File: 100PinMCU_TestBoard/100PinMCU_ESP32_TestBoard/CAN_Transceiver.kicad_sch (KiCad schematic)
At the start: 9 parts, among them IC1 TCAN3413DR

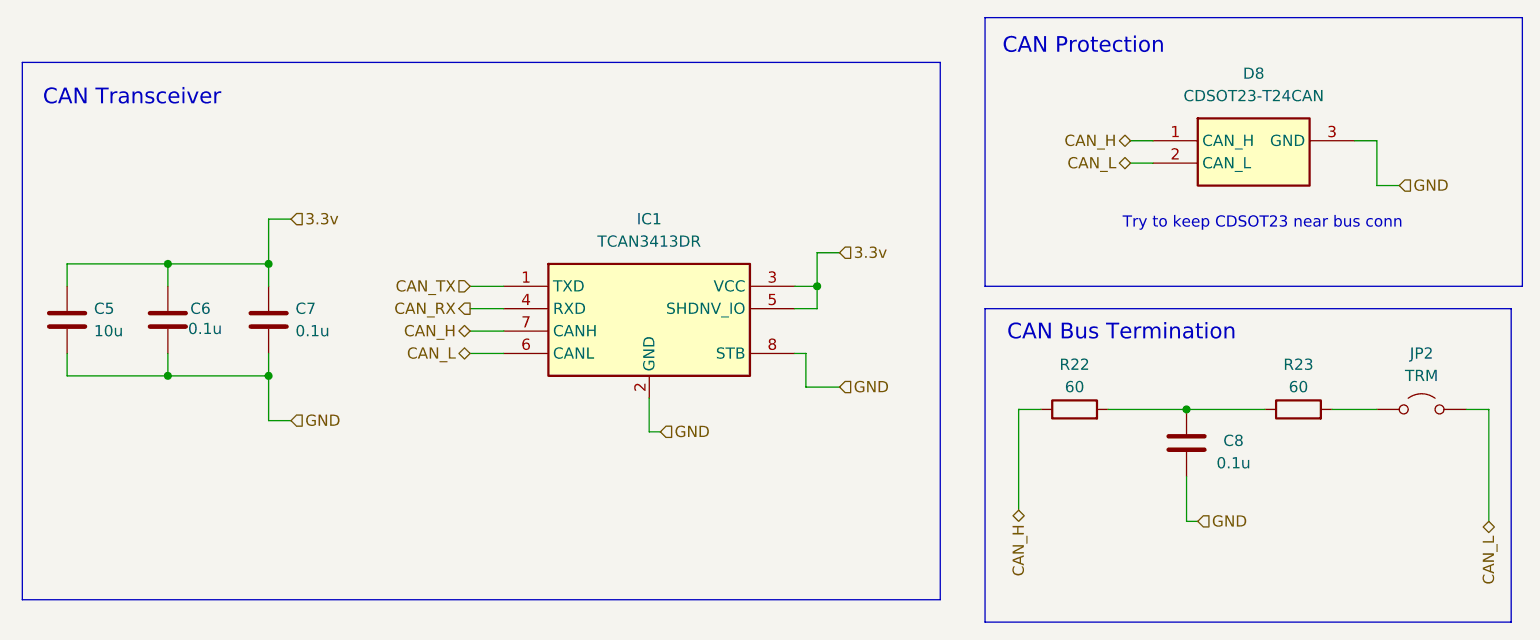
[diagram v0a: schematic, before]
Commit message: esp32 design block will be updated later
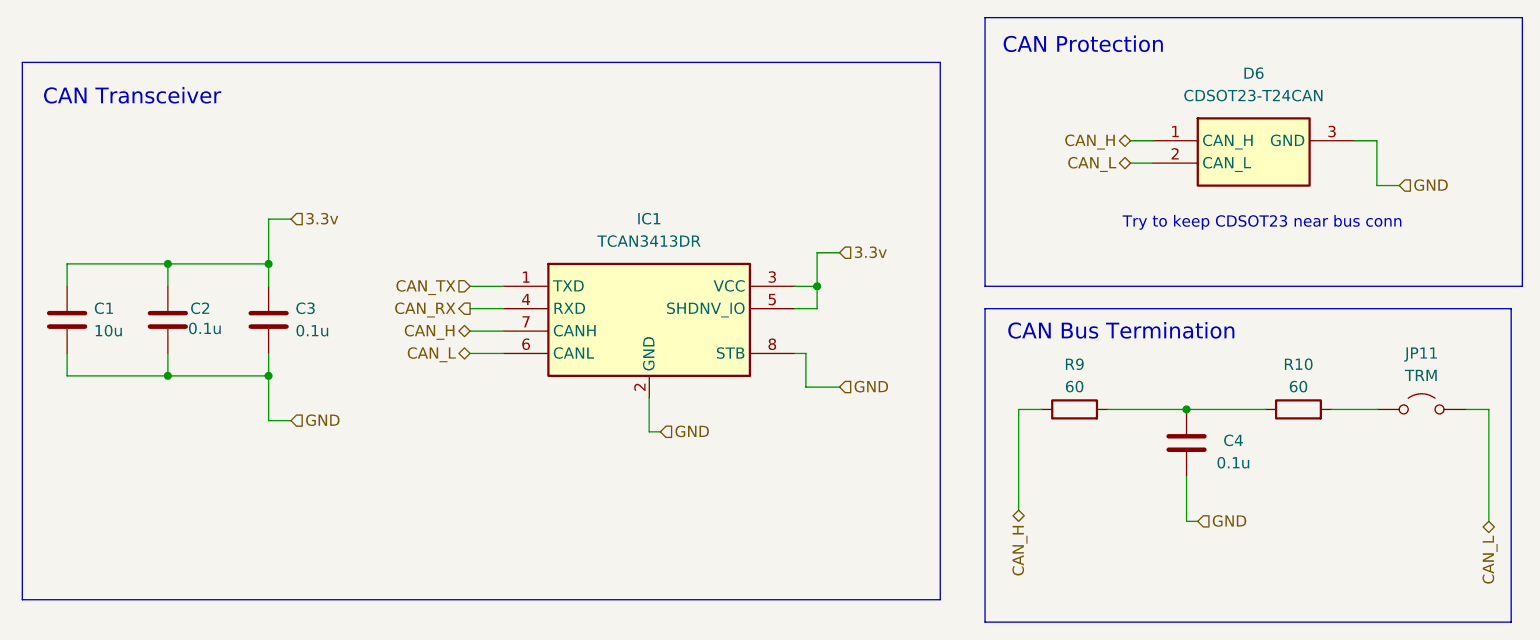
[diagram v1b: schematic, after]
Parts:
- renumbered C5 to C1, C6 to C2, C7 to C3, C8 to C4, D8 to D6, JP2 to JP11, R23 to R10, R22 to R9
